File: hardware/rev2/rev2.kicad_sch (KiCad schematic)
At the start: 29 parts, among them J1 USB_C_Receptacle_USB2.0_16P, J2 uFL, J3 uFL, J4 Antenna RF and GNSS Data, J5 Antenna GND, U1 EClamp2522P

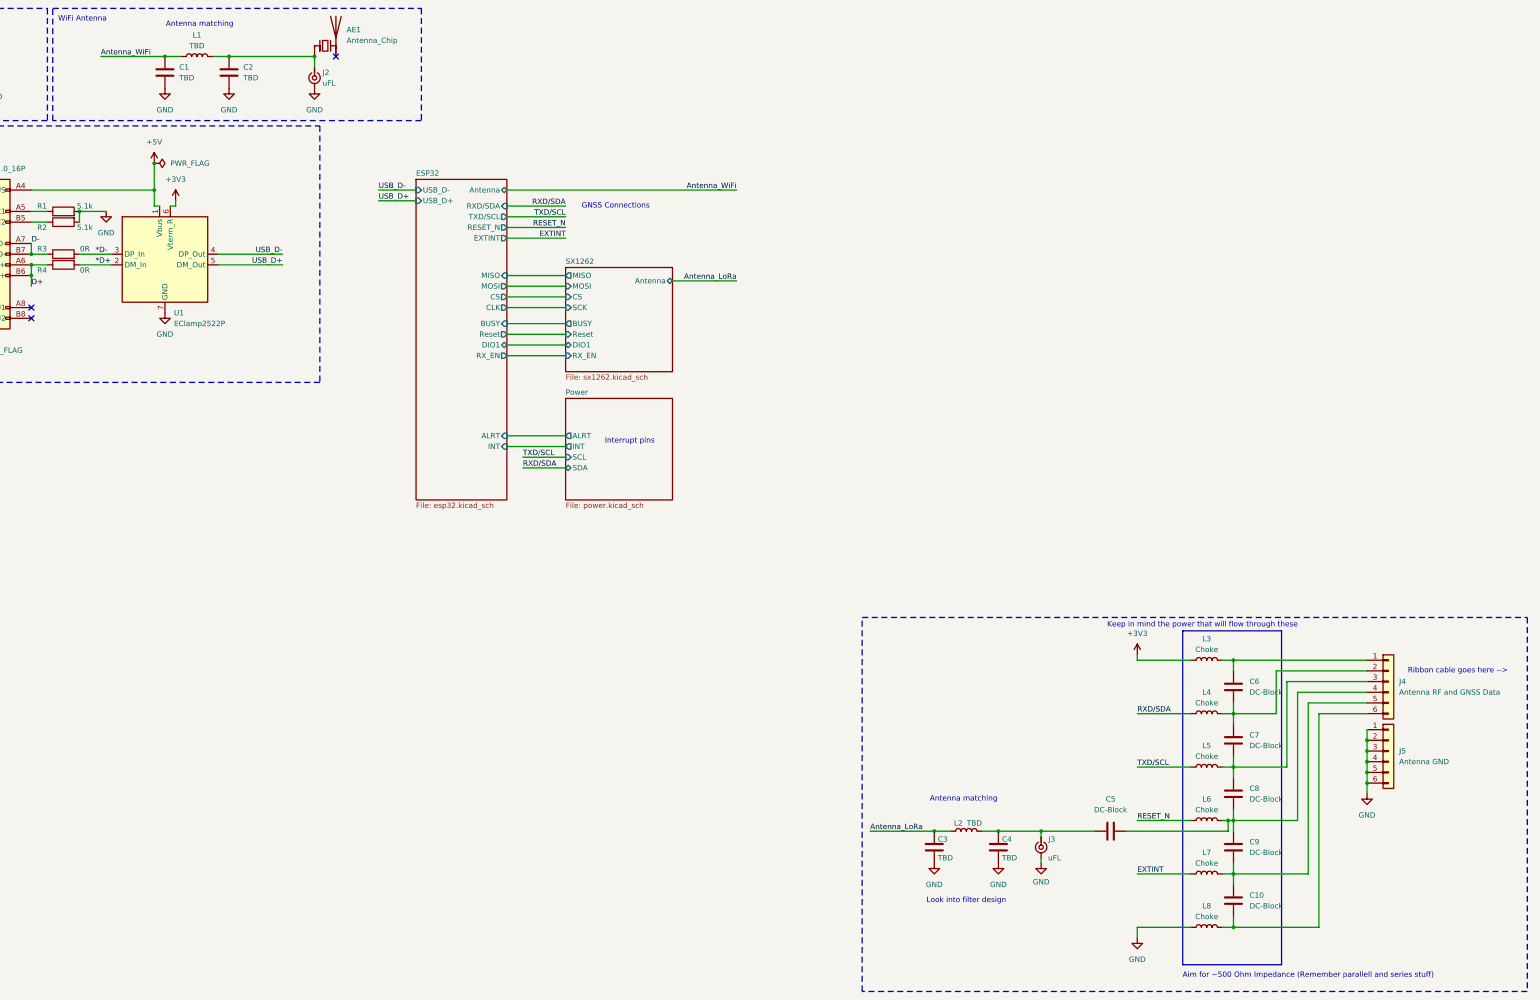
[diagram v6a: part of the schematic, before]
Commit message: routed everything ESP32 and SX1262, will hopefully work. still needs more testpoints
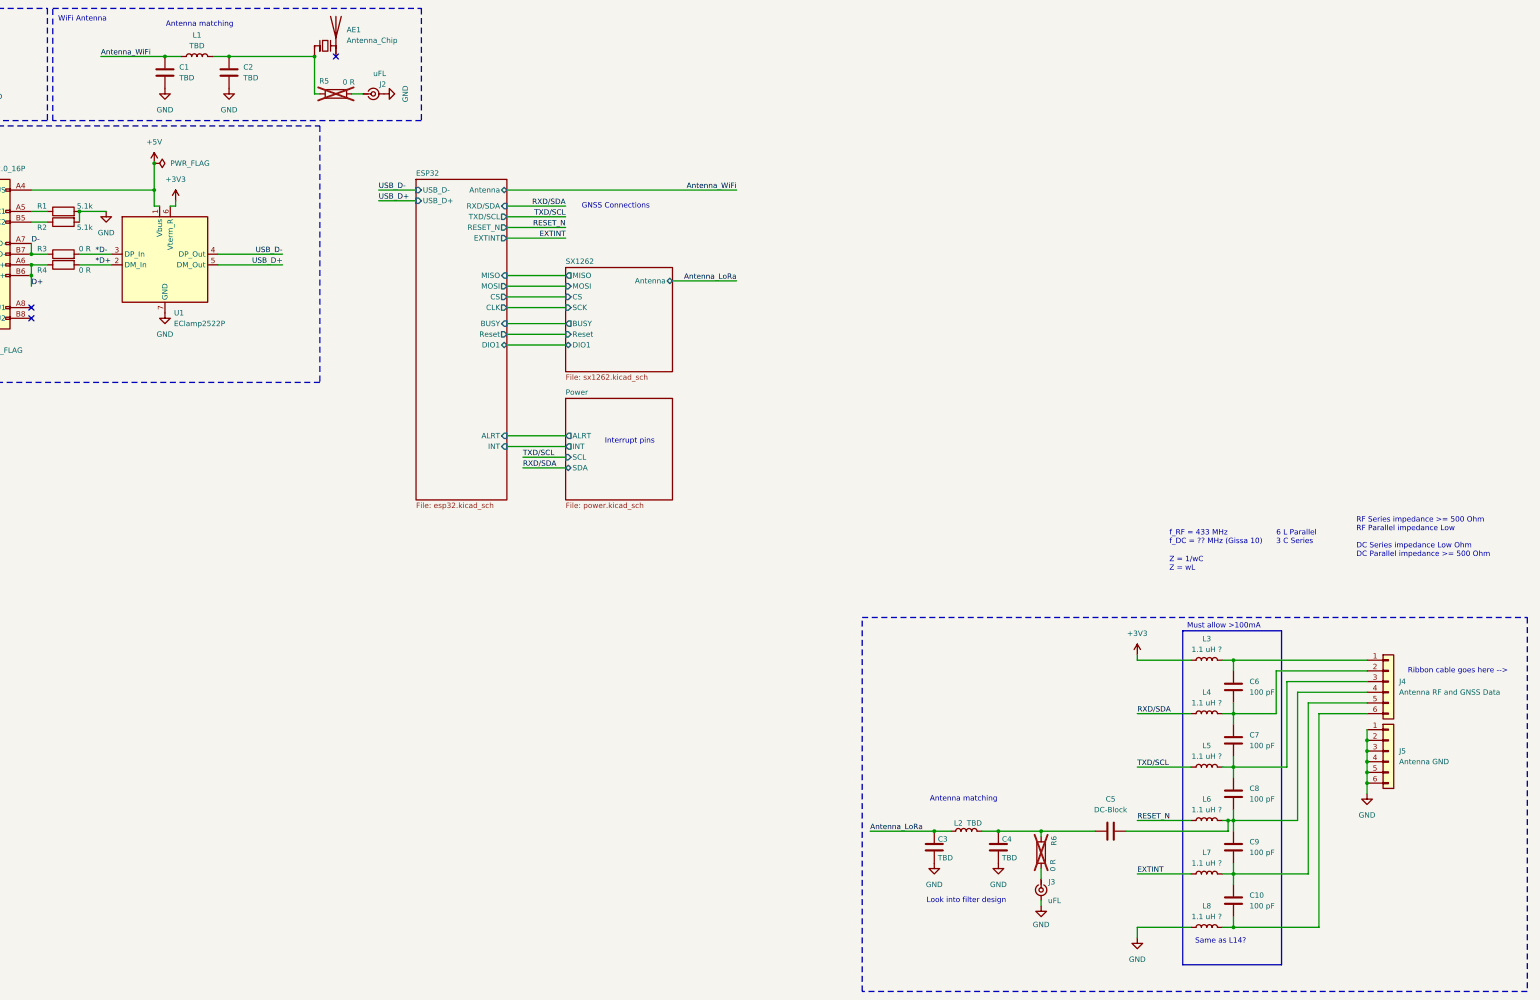
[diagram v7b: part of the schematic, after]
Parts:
- added R5, R6: 0 R, Resistor_SMD:R_0402_1005Metric_Pad0.72x0.64mm_HandSolder, symbol Device:R
- C10, C6, C7, C8, C9: value DC-Block -> 100 pF
- J2, J3: footprint Connector_Coaxial:SMA_Amphenol_132134-16_Vertical -> _footprints:U.FL_Molex_MCRF_73412-0110_Vertical; Mouser Part Number 640-RFPCSMA28F -> 712-CONMHF1-SMD-G-T
- L3, L4, L5, L6, L7, L8: value Choke -> 1.1 uH ?; Mouser Part Number (none) -> 710-744230251 ?
- R3, R4: value 0R -> 0 R; Mouser Part Number (none) -> 71-CRCW0603-0-E3
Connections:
- net at AE1.1 (FEED), C2.1, L1.1: now also R5.1; no longer J2.1 (In)
- net at C4.1, C5.1, L2.1: now also R6.1; no longer J3.1 (In)
- new net: J2.1 (In), R5.2
- new net: J3.1 (In), R6.2
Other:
- sheet ESP32 ports: added none; removed RX_EN
- sheet SX1262 ports: added none; removed RX_EN
- note added: "6 L Parallel 3 C Series"
- note added: "Must allow >100mA"
- note added: "RF Series impedance >= 500 Ohm RF Parallel impedance Low DC Series impedance Low Ohm DC Parallel impedance >= 500 Ohm"
- note added: "Same as L14?"
- note added: "Z = 1/wC Z = wL"
- note added: "f_RF = 433 MHz f_DC = ?? MHz (Gissa 10)"
- note removed: "Aim for ~500 Ohm Impedance (Remember parallell and series stuff)"
- note removed: "Keep in mind the power that will flow through these"
- moved on the sheet: J2, J3
